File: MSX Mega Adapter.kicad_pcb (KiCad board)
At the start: 2 copper layers, 30.5 x 31.8 mm, 6 parts, among them J1 MSX, J2 Mega Drive, U1 74HCT04

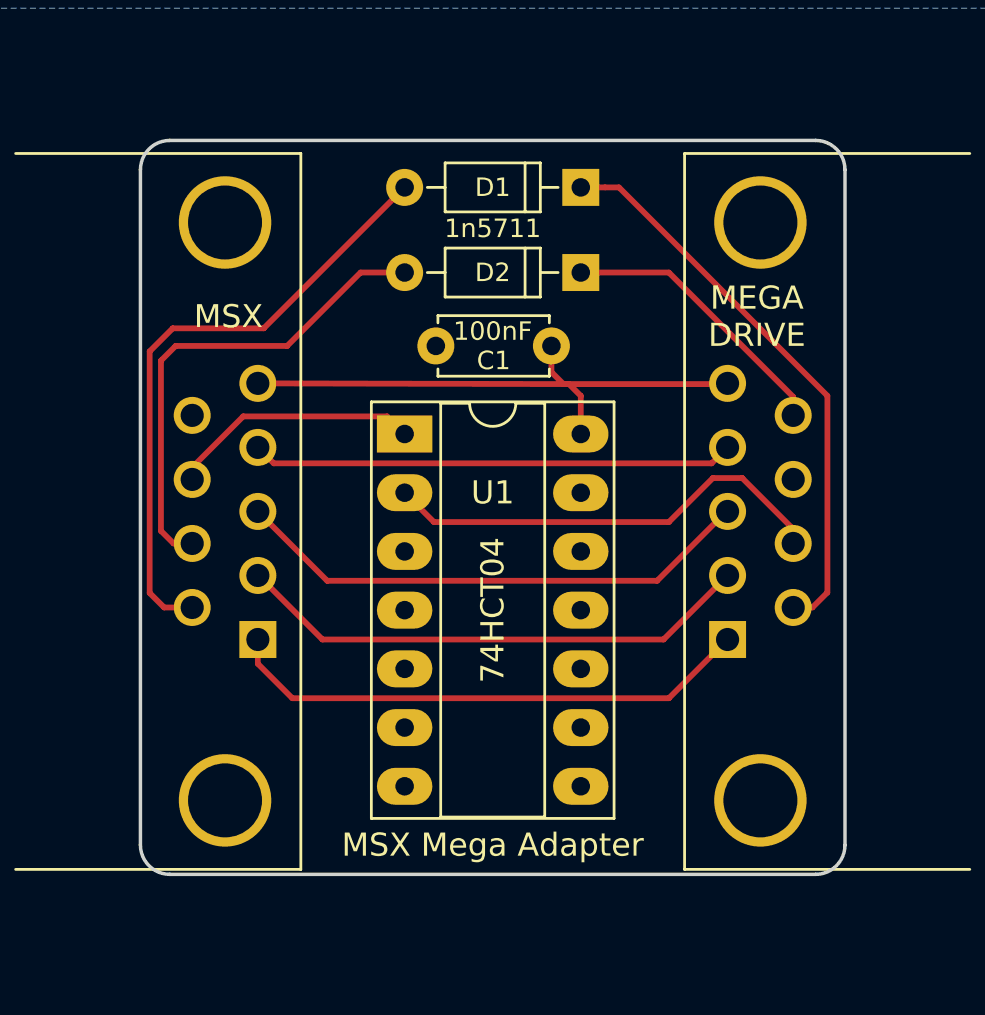
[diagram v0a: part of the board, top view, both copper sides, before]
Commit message: UPD: Updated KiCAD project to v6.0 - Also changed 3D objects references to default KiCAD6 paths, so no   extra modules are required
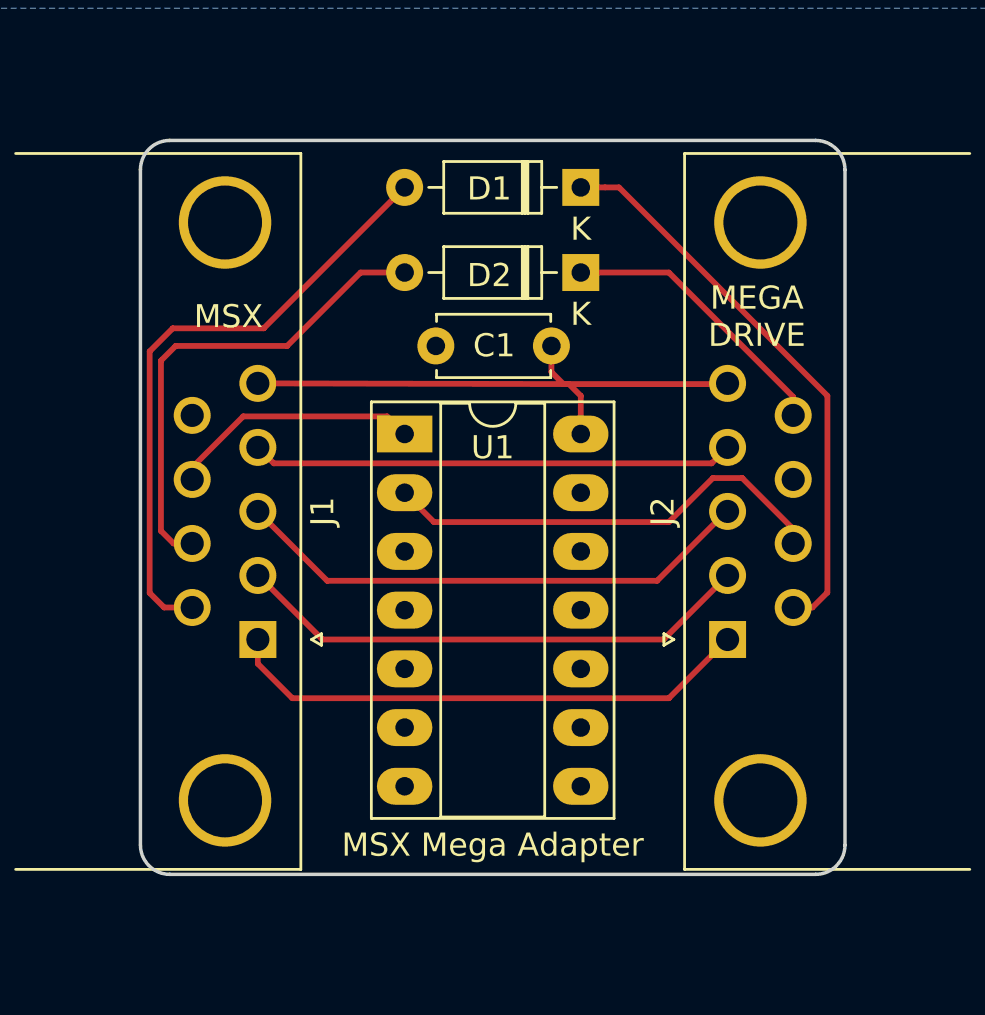
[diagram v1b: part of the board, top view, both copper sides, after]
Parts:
- C1: footprint Capacitors_THT:C_Disc_D4.7mm_W2.5mm_P5.00mm -> Capacitor_THT:C_Disc_D4.7mm_W2.5mm_P5.00mm
- D1, D2: footprint Diodes_THT:D_DO-35_SOD27_P7.62mm_Horizontal -> Diode_THT:D_DO-35_SOD27_P7.62mm_Horizontal
- J1: footprint RND:DSUB-9_Female_Horizontal_P2.77x2.84mm_EdgePinOffset7.70mm_Housed_MountingHolesOffset9.12mm -> Connector_Dsub:DSUB-9_Female_Horizontal_P2.77x2.84mm_EdgePinOffset7.70mm_Housed_MountingHolesOffset9.12mm
- J2: footprint RND:DSUB-9_Male_Horizontal_P2.77x2.84mm_EdgePinOffset7.70mm_Housed_MountingHolesOffset9.12mm -> Connector_Dsub:DSUB-9_Male_Horizontal_P2.77x2.84mm_EdgePinOffset7.70mm_Housed_MountingHolesOffset9.12mm
- U1: footprint Housings_DIP:DIP-14_W7.62mm_Socket_LongPads -> Package_DIP:DIP-14_W7.62mm_Socket_LongPads
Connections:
- U1 pad 10: (no net) -> unconnected-(U1-Pad10)
- U1 pad 12: (no net) -> unconnected-(U1-Pad12)
- U1 pad 4: (no net) -> unconnected-(U1-Pad4)
- U1 pad 6: (no net) -> unconnected-(U1-Pad6)
- U1 pad 8: (no net) -> unconnected-(U1-Pad8)
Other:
- net class Default removed
- net class Power removed
